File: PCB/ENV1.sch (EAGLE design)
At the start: 46 parts, among them IC1 78L05, IC2 4066D, IC3 MCP6002, IC4 TL072D, SW1 TL2285, T1 BC847

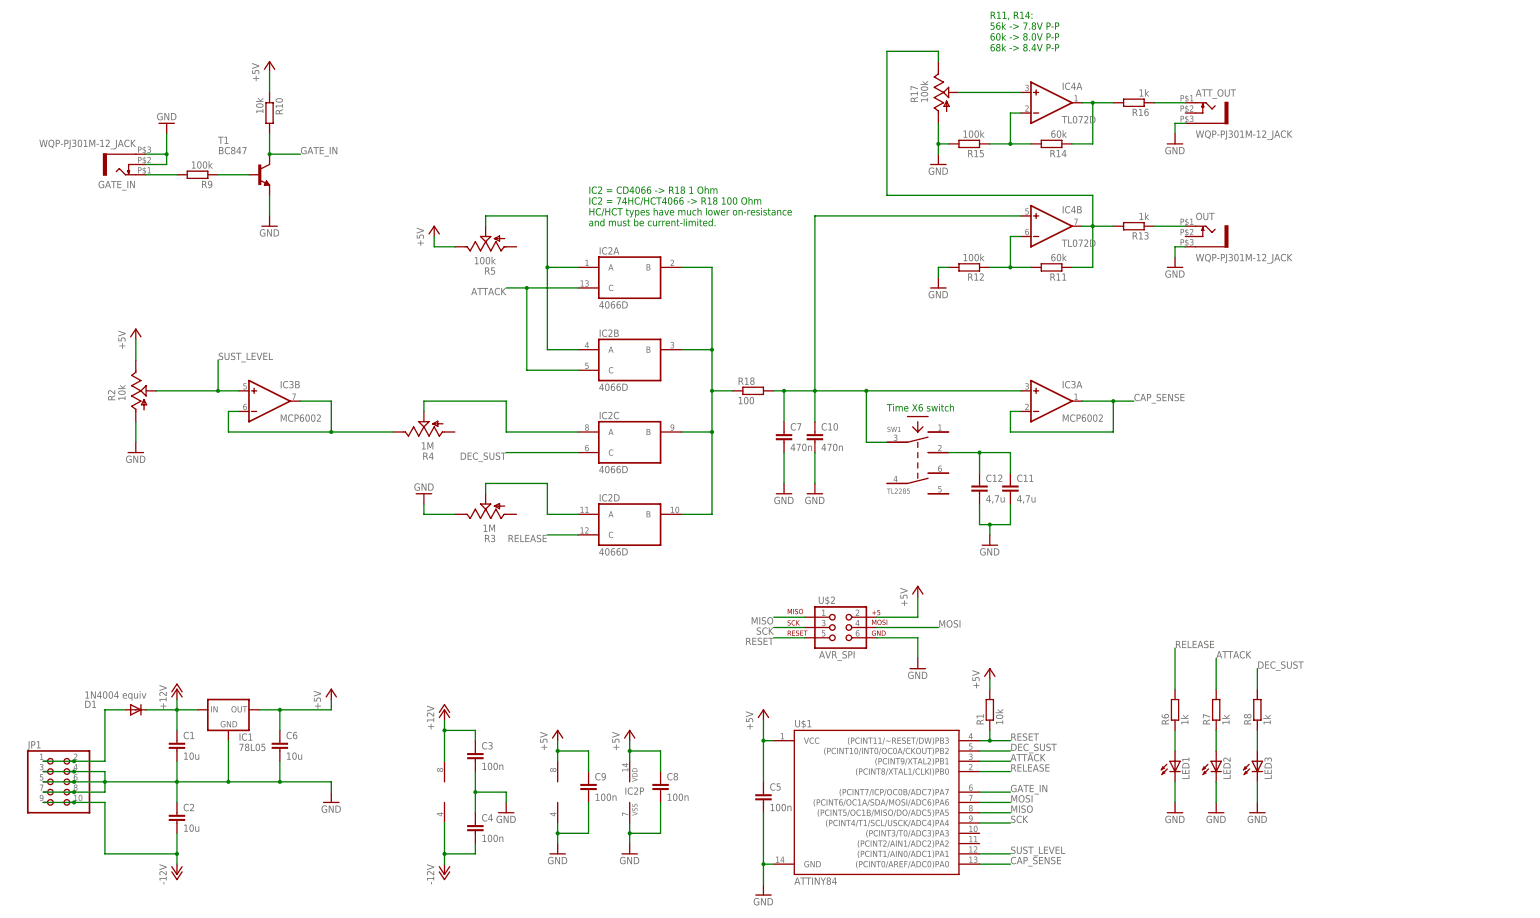
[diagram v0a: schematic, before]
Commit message: Value adjustments for timing capacitors. Added forgotten diode in -12V supply.
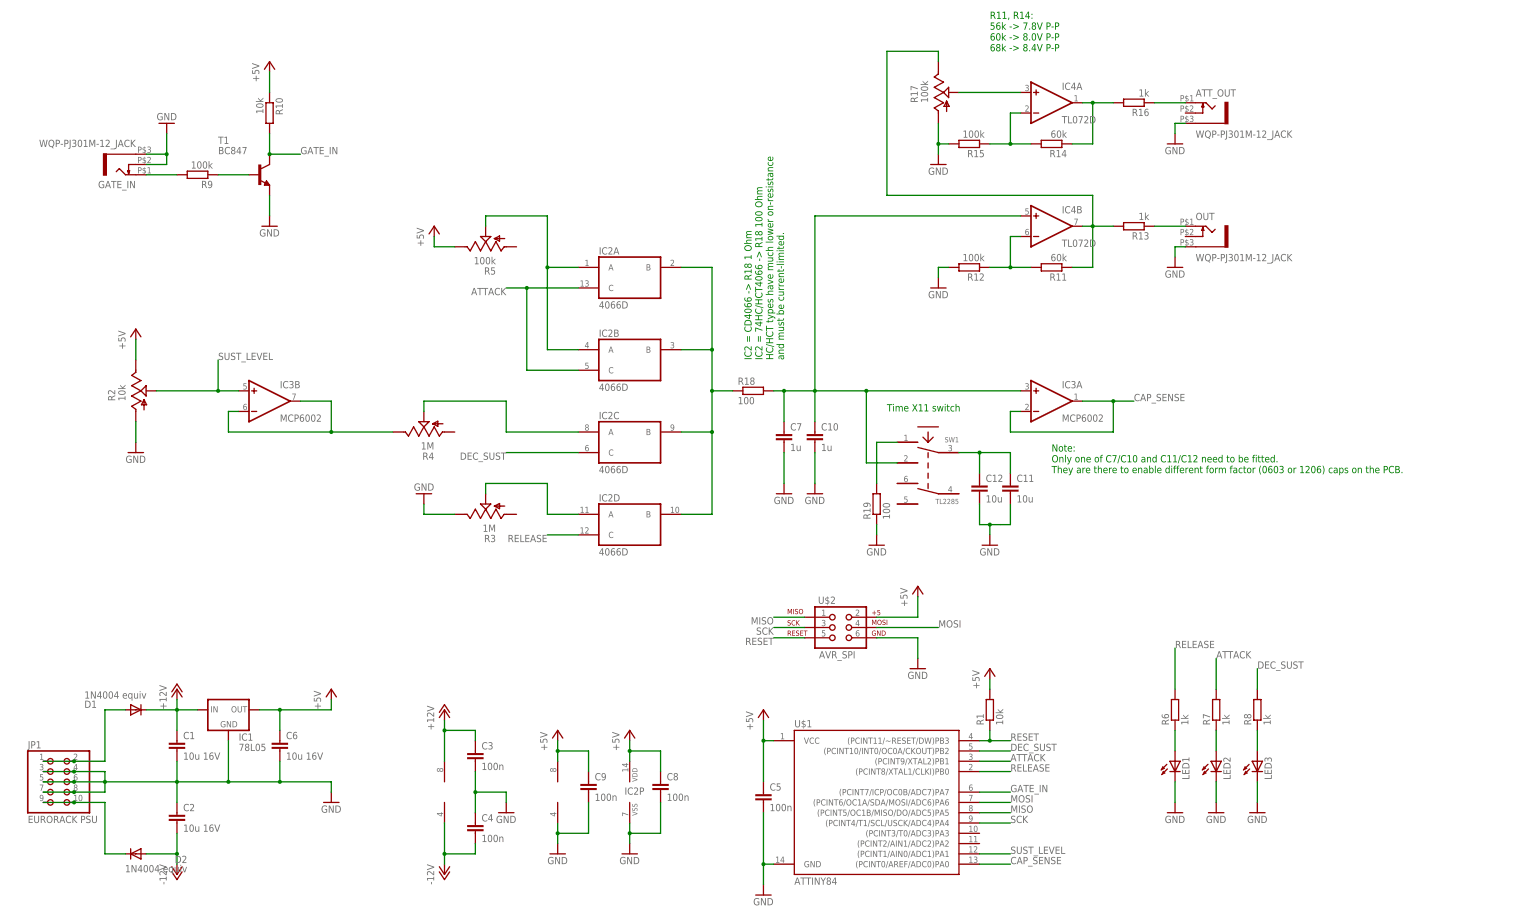
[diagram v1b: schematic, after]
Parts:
- added D2: 1N4004 equiv, diode:DIODE-DO214AA
- added R19: 100, rcl:R-EU_R0603
- C1, C2, C6: value 10u -> 10u 16V
- C10, C7: value 470n -> 1u
- C11, C12: value 4,7u -> 10u
- JP1: value (none) -> EURORACK PSU
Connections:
- new net N$14: D2.C, JP1.10, JP1.9
- new net N$18: R19.2, SW1.P1
- net -12V: now also D2.A; no longer JP1.10, JP1.9
- net GND: now also R19.1
- net N$1: now also SW1.P2; no longer SW1.P3
- net N$16: now also SW1.P3; no longer SW1.P2
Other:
- note added: "Note: Only one of C7/C10 and C11/C12 need to be fitted. They are there to enable different form factor (0603 or 1206) caps on the PCB."
- note added: "Time X11 switch"
- note removed: "Time X6 switch"
- moved on the sheet: SW1
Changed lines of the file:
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@@
 <part name="FRAME1" library="frames" deviceset="A3L-LOC" device=""/>
 <part name="U$1" library="SparkFun-DigitalIC" deviceset="ATTINY84" device=""/>
-<part name="JP1" library="pinhead" deviceset="PINHD-2X5" device=""/>
+<part name="JP1" library="pinhead" deviceset="PINHD-2X5" device="" value="EURORACK PSU"/>
 <part name="C5" library="rcl" deviceset="C-EU" device="C0603K" value="100n"/>
 <part name="IC1" library="lb_devs" deviceset="78LXX" device="SMD" value="78L05"/>
@@
 <part name="IC2" library="40xx" deviceset="4066" device="D"/>
 <part name="IC3" library="linear" deviceset="TL072" device="D" value="MCP6002"/>
-<part name="C7" library="rcl" deviceset="C-EU" device="C0603K" value="470n"/>
+<part name="C7" library="rcl" deviceset="C-EU" device="C0603K" value="1u"/>
 <part name="GND4" library="supply1" deviceset="GND" device=""/>
 <part name="P+6" library="supply1" deviceset="+5V" device=""/>
@@
 <part name="GND10" library="supply1" deviceset="GND" device=""/>
 <part name="GND11" library="supply1" deviceset="GND" device=""/>
-<part name="C10" library="rcl" deviceset="C-EU" device="C1206K" value="470n"/>
+<part name="C10" library="rcl" deviceset="C-EU" device="C1206K" value="1u"/>
 <part name="GND12" library="supply1" deviceset="GND" device=""/>
 <part name="GATE_IN" library="thonkiconn" deviceset="WQP-PJ301M-12_JACK" device=""/>
@@
 <part name="GND13" library="supply1" deviceset="GND" device=""/>
 <part name="GND14" library="supply1" deviceset="GND" device=""/>
-<part name="C6" library="rcl" deviceset="C-EU" device="C1206K" value="10u"/>
-<part name="C1" library="rcl" deviceset="C-EU" device="C1206K" value="10u"/>
-<part name="C2" library="rcl" deviceset="C-EU" device="C1206K" value="10u"/>
+<part name="C6" library="rcl" deviceset="C-EU" device="C1206K" value="10u 16V"/>
+<part name="C1" library="rcl" deviceset="C-EU" device="C1206K" value="10u 16V"/>
+<part name="C2" library="rcl" deviceset="C-EU" device="C1206K" value="10u 16V"/>
 <part name="IC4" library="linear" deviceset="TL072" device="D"/>
 <part name="R11" library="rcl" deviceset="R-EU_" device="R0603" value="60k"/>
@@
 <part name="GND17" library="supply1" deviceset="GND" device=""/>
 <part name="SW1" library="lb_devs" deviceset="TL2285" device=""/>
-<part name="C11" library="rcl" deviceset="C-EU" device="C1206K" value="4,7u"/>
-<part name="C12" library="rcl" deviceset="C-EU" device="C0603K" value="4,7u"/>
+<part name="C11" library="rcl" deviceset="C-EU" device="C1206K" value="10u"/>
+<part name="C12" library="rcl" deviceset="C-EU" device="C0603K" value="10u"/>
 <part name="GND18" library="supply1" deviceset="GND" device=""/>
 <part name="R14" library="rcl" deviceset="R-EU_" device="R0603" value="60k"/>
@@
 <part name="R17" library="pot-alps" deviceset="POT_US" device="VERTICAL" value="100k"/>
 <part name="R18" library="rcl" deviceset="R-EU_" device="R0603" value="100"/>
+<part name="R19" library="rcl" deviceset="R-EU_" device="R0603" value="100"/>
+<part name="GND21" library="supply1" deviceset="GND" device=""/>
+<part name="D2" library="diode" deviceset="DIODE-" device="DO214AA" value="1N4004 equiv"/>
 </parts>
 <sheets>
@@
 60k -&gt; 8.0V P-P
 68k -&gt; 8.4V P-P</text>
-<text x="228.6" y="139.7" size="1.778" layer="91">Time X6 switch</text>
-<text x="154.94" y="185.42" size="1.778" layer="91">IC2 = CD4066 -&gt; R18 1 Ohm
+<text x="228.6" y="139.7" size="1.778" layer="91">Time X11 switch</text>
+<text x="203.2" y="152.4" size="1.778" layer="91" rot="R90">IC2 = CD4066 -&gt; R18 1 Ohm
 IC2 = 74HC/HCT4066 -&gt; R18 100 Ohm
 HC/HCT types have much lower on-resistance
 and must be current-limited.</text>
+<text x="269.24" y="124.46" size="1.778" layer="91">Note:
+Only one of C7/C10 and C11/C12 need to be fitted.
+They are there to enable different form factor (0603 or 1206) caps on the PCB.</text>
 </plain>
 <instances>
@@
 <instance part="P-2" gate="1" x="119.38" y="25.4"/>
 <instance part="GND17" gate="1" x="134.62" y="40.64"/>
-<instance part="SW1" gate="G$1" x="236.22" y="127"/>
+<instance part="SW1" gate="G$1" x="238.76" y="124.46" rot="MR0"/>
 <instance part="C11" gate="G$1" x="259.08" y="121.92"/>
 <instance part="C12" gate="G$1" x="251.46" y="121.92"/>
@@
 <instance part="R17" gate="G$1" x="241.3" y="218.44"/>
 <instance part="R18" gate="G$1" x="195.58" y="144.78"/>
+<instance part="R19" gate="G$1" x="226.06" y="116.84" rot="R90"/>
+<instance part="GND21" gate="1" x="226.06" y="106.68"/>
+<instance part="D2" gate="G$1" x="43.18" y="30.48" smashed="yes" rot="R180">
+<attribute name="NAME" x="55.88" y="29.9974" size="1.778" layer="95" rot="R180"/>
+<attribute name="VALUE" x="55.88" y="27.7114" size="1.778" layer="96" rot="R180"/>
+</instance>
 </instances>
 <busses>
@@
 <junction x="241.3" y="205.74"/>
 </segment>
+<segment>
+<pinref part="GND21" gate="1" pin="GND"/>
+<pinref part="R19" gate="G$1" pin="1"/>
+<wire x1="226.06" y1="109.22" x2="226.06" y2="111.76" width="0.1524" layer="91"/>
+</segment>
 </net>
 <net name="+12V" class="0">
@@
 <net name="-12V" class="0">
 <segment>
-<pinref part="JP1" gate="A" pin="9"/>
-<pinref part="JP1" gate="A" pin="10"/>
-<wire x1="20.32" y1="43.18" x2="27.94" y2="43.18" width="0.1524" layer="91"/>
-<wire x1="27.94" y1="43.18" x2="35.56" y2="43.18" width="0.1524" layer="91"/>
-<wire x1="35.56" y1="43.18" x2="35.56" y2="30.48" width="0.1524" layer="91"/>
-<junction x="27.94" y="43.18"/>
-<wire x1="35.56" y1="30.48" x2="53.34" y2="30.48" width="0.1524" layer="91"/>
 <pinref part="P-1" gate="1" pin="-12V"/>
-<wire x1="53.34" y1="27.94" x2="53.34" y2="30.48" width="0.1524" layer="91"/>
+<pinref part="C2" gate="G$1" pin="2"/>
 <wire x1="53.34" y1="35.56" x2="53.34" y2="30.48" width="0.1524" layer="91"/>
+<pinref part="D2" gate="G$1" pin="A"/>
+<wire x1="53.34" y1="30.48" x2="53.34" y2="27.94" width="0.1524" layer="91"/>
+<wire x1="45.72" y1="30.48" x2="53.34" y2="30.48" width="0.1524" layer="91"/>
 <junction x="53.34" y="30.48"/>
-<pinref part="C2" gate="G$1" pin="2"/>
 </segment>
 <segment>
@@
 <wire x1="261.62" y1="187.96" x2="210.82" y2="187.96" width="0.1524" layer="91"/>
 <wire x1="210.82" y1="187.96" x2="210.82" y2="144.78" width="0.1524" layer="91"/>
-<pinref part="SW1" gate="G$1" pin="P3"/>
-<wire x1="228.6" y1="132.08" x2="223.52" y2="132.08" width="0.1524" layer="91"/>
-<wire x1="223.52" y1="132.08" x2="223.52" y2="144.78" width="0.1524" layer="91"/>
+<wire x1="223.52" y1="127" x2="223.52" y2="144.78" width="0.1524" layer="91"/>
 <junction x="223.52" y="144.78"/>
 <pinref part="R18" gate="G$1" pin="2"/>
 <wire x1="200.66" y1="144.78" x2="203.2" y2="144.78" width="0.1524" layer="91"/>
 <junction x="203.2" y="144.78"/>
+<pinref part="SW1" gate="G$1" pin="P2"/>
+<wire x1="231.14" y1="127" x2="223.52" y2="127" width="0.1524" layer="91"/>
 </segment>
 </net>
@@
 <net name="N$16" class="0">
 <segment>
-<pinref part="SW1" gate="G$1" pin="P2"/>
-<wire x1="243.84" y1="129.54" x2="251.46" y2="129.54" width="0.1524" layer="91"/>
 <pinref part="C12" gate="G$1" pin="1"/>
 <wire x1="251.46" y1="129.54" x2="251.46" y2="124.46" width="0.1524" layer="91"/>
@@
 <pinref part="C11" gate="G$1" pin="1"/>
 <wire x1="259.08" y1="129.54" x2="259.08" y2="124.46" width="0.1524" layer="91"/>
+<pinref part="SW1" gate="G$1" pin="P3"/>
+<wire x1="246.38" y1="129.54" x2="251.46" y2="129.54" width="0.1524" layer="91"/>
 <junction x="251.46" y="129.54"/>
 </segment>
@@
 </segment>
 </net>
+<net name="N$18" class="0">
+<segment>
+<pinref part="SW1" gate="G$1" pin="P1"/>
+<wire x1="231.14" y1="132.08" x2="226.06" y2="132.08" width="0.1524" layer="91"/>
+<wire x1="226.06" y1="132.08" x2="226.06" y2="121.92" width="0.1524" layer="91"/>
+<pinref part="R19" gate="G$1" pin="2"/>
+</segment>
+</net>
+<net name="N$14" class="0">
+<segment>
+<pinref part="JP1" gate="A" pin="9"/>
+<pinref part="JP1" gate="A" pin="10"/>
+<wire x1="20.32" y1="43.18" x2="27.94" y2="43.18" width="0.1524" layer="91"/>
+<wire x1="27.94" y1="43.18" x2="35.56" y2="43.18" width="0.1524" layer="91"/>
+<wire x1="35.56" y1="43.18" x2="35.56" y2="30.48" width="0.1524" layer="91"/>
+<junction x="27.94" y="43.18"/>
+<pinref part="D2" gate="G$1" pin="C"/>
+<wire x1="40.64" y1="30.48" x2="35.56" y2="30.48" width="0.1524" layer="91"/>
+</segment>
+</net>

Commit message: Added handling of 74HC4017 counter chip that manages the UI LEDs. Added same chip to schematic.
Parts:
- R18, R19: device rcl:R-EU_R0603 -> rcl:R-EU_R1206
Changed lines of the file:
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@@
 <part name="GND20" library="supply1" deviceset="GND" device=""/>
 <part name="R17" library="pot-alps" deviceset="POT_US" device="VERTICAL" value="100k"/>
-<part name="R18" library="rcl" deviceset="R-EU_" device="R0603" value="100"/>
-<part name="R19" library="rcl" deviceset="R-EU_" device="R0603" value="100"/>
+<part name="R18" library="rcl" deviceset="R-EU_" device="R1206" value="100"/>
+<part name="R19" library="rcl" deviceset="R-EU_" device="R1206" value="100"/>
 <part name="GND21" library="supply1" deviceset="GND" device=""/>
 <part name="D2" library="diode" deviceset="DIODE-" device="DO214AA" value="1N4004 equiv"/>
